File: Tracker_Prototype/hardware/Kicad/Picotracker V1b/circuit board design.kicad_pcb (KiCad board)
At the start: 2 copper layers, 33.3 x 20.1 mm, 30 parts, among them J1 Conn_01x06, J2 GND, J3 3.3V, SW1 SW_Push, U1 MAX-M8C, U3 CMWX1ZZABZ-078, U6 MS5607-02BA

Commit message: updated the "b" variant
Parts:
- removed AE2: GPS Antenna, Connector_Wire:SolderWirePad_1x01_Drill0.8mm
- removed C12: 100nF, Capacitor_SMD:C_0402_1005Metric
- removed C13: 10uF, Capacitor_SMD:C_0603_1608Metric
- removed G***: LOGO, flight-computer:ICSS_Logo
- removed R1, R2: 100K, Resistor_SMD:R_0402_1005Metric
- removed U1: MAX-M8C, RF_GPS:ublox_MAX
- added IC7: SPV1040, Package_SO:TSSOP-8_4.4x3mm_P0.65mm, F.Cu at (286.9, 151.4)
- added J4: Conn_01x01, Connector_PinHeader_1.27mm:PinHeader_1x01_P1.27mm_Vertical, F.Cu at (293.5, 150.8)
- J3: value 3.3V -> +SOL
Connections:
- J3 pad 1: +3V3 -> +SOL
- U3 pad 15: /GPS_TIMEPULSE -> (no net)
- U3 pad 16: /GPS_EXTINT -> (no net)
- U3 pad 17: /GPS_SAFEBOOT -> (no net)
- U3 pad 24: /V_SOLAR -> (no net)
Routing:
- net /GPS_EXTINT: track 10.0 -> 0.00 mm
- net /GPS_SAFEBOOT: track 9.36 -> 0.00 mm
- net /GPS_TIMEPULSE: track 8.59 -> 0.00 mm
- net GND: track 79.3 -> 72.8 mm
- net Net-(AE2-Pad1): track 6.23 -> 0.00 mm
- net /V_SOLAR: track 4.84 -> 0.00 mm
- net (no net): track 0.00 -> 4.84 mm
- net /I2C1_SCL: track 26.8 -> 23.3 mm
- net +3V3: track 79.5 -> 77.1 mm

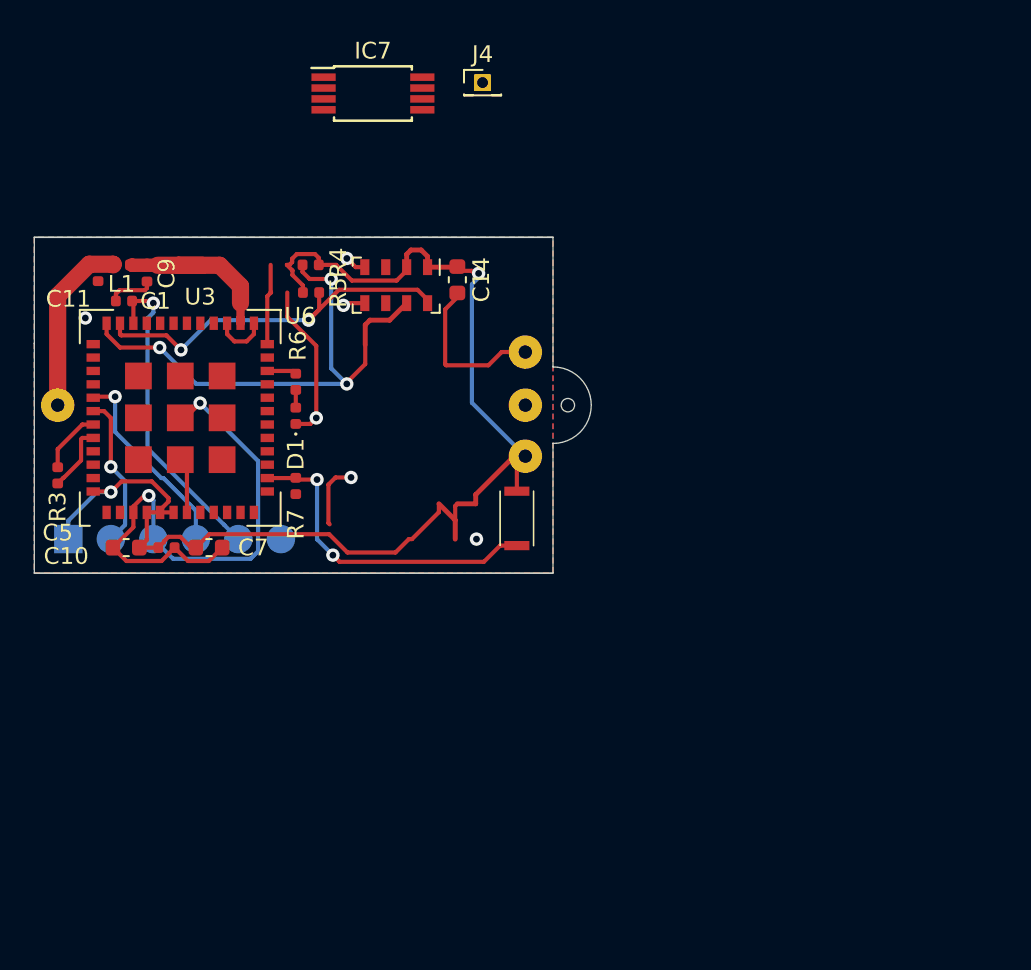
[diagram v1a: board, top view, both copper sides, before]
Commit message: mostly wired up the "b" variant. Changed the fill clearance for copper pour for the "a" variant to a much smaller 0.15mm
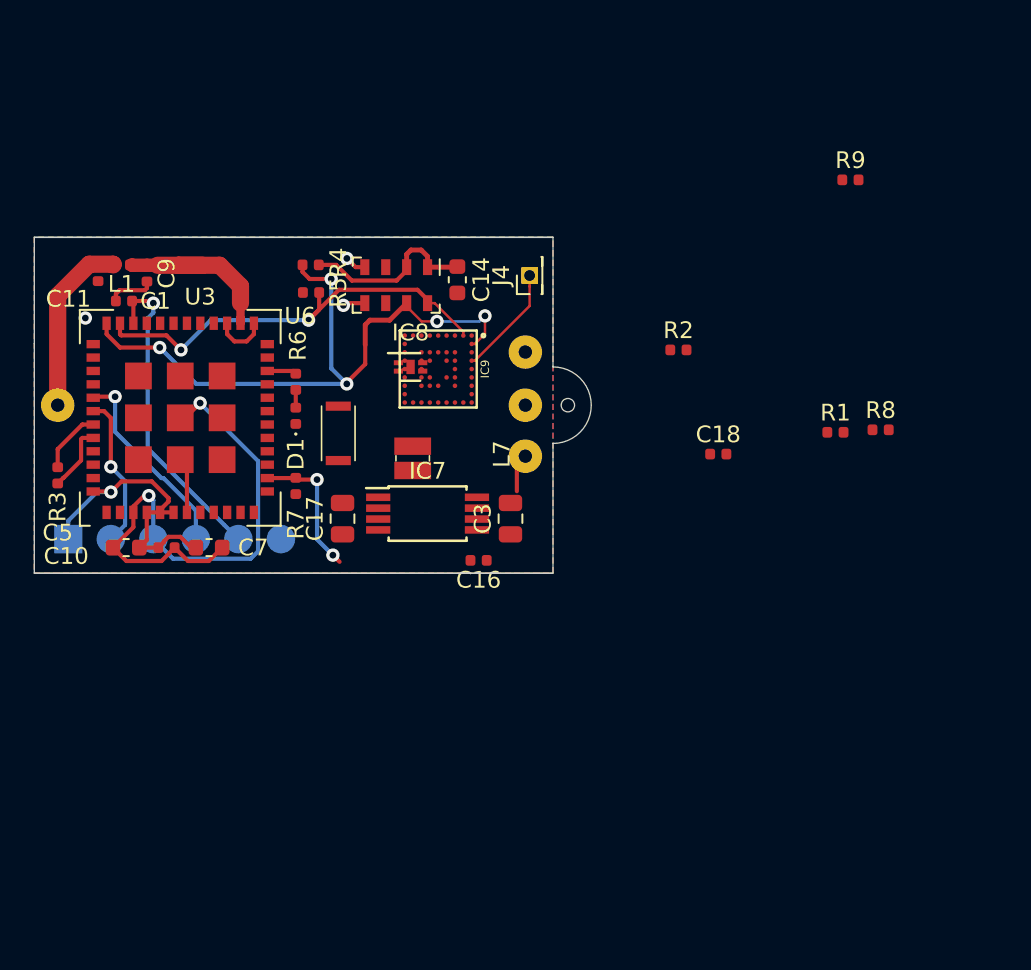
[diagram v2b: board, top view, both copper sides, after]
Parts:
- added C16: 1n, Capacitor_SMD:C_0402_1005Metric, F.Cu at (293.2, 179.3)
- added C17: 22u, Capacitor_SMD:C_0805_2012Metric, F.Cu at (285.1, 176.8)
- added C18: 100n, Capacitor_SMD:C_0402_1005Metric, F.Cu at (307.6, 173.0)
- added C3: 22u, Capacitor_SMD:C_0805_2012Metric, F.Cu at (295.1, 176.8)
- added IC8: SIP32431DNP3-T1GE4, pecanpico:DFN-4-1EP_1.2x1.6mm_P0.5mm_EP, F.Cu at (289.2, 167.8)
- added IC9: ZOE-M8G/B, pecanpico:ZOE-M8, F.Cu at (290.8, 167.9)
- added L7: XFL2006-472MEB, pecanpico:XFL20xx, F.Cu at (289.3, 173.2)
- added R1: R, Resistor_SMD:R_0402_1005Metric, F.Cu at (314.6, 171.7)
- added R2: 10K, Resistor_SMD:R_0402_1005Metric, F.Cu at (305.2, 166.8)
- added R8: R, Resistor_SMD:R_0402_1005Metric, F.Cu at (317.3, 171.5)
- added R9: 10K, Resistor_SMD:R_0402_1005Metric, F.Cu at (315.5, 156.6)
- moved IC7 25.3 mm to (290.2, 176.5)
- moved J4 11.9 mm to (296.3, 162.3), turned to 90 degrees
- moved SW1 11.8 mm to (284.9, 172.2)
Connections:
- IC7 pad 3: (no net) -> Net-(IC7-Pad3)
- IC7 pad 5: (no net) -> Net-(C16-Pad2)
- J4 pad 1: (no net) -> Net-(IC9-PadA4)
- U3 pad 16: (no net) -> /GPS_EXTINT
- U3 pad 17: (no net) -> /GPS_SAFEBOOT
- U3 pad 24: (no net) -> /V_SOLAR
- U3 pad 38: (no net) -> /GPS_EN
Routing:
- net +3V3: track 77.1 -> 29.0 mm, vias 2 -> 1
- net GND: track 72.8 -> 49.8 mm, vias 8 -> 5
- net /SWITCH: track 19.5 -> 8.49 mm
- net /I2C1_SDA: track 32.2 -> 39.7 mm, vias 3 -> 5
- net Net-(IC9-PadA4): track 0.00 -> 6.63 mm
- net (no net): track 4.84 -> 0.00 mm
- net /I2C1_SCL: track 23.3 -> 26.3 mm
- net +SOL: track 0.00 -> 2.30 mm
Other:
- rule trace_min: 0.2 -> 0.15
- rule via_min_drill: 0.3 -> 0.2
- rule via_min_size: 0.4 -> 0.45

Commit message: updated circuit of b variant for low power voltage measurment. Made a variant tcxo enable controllable
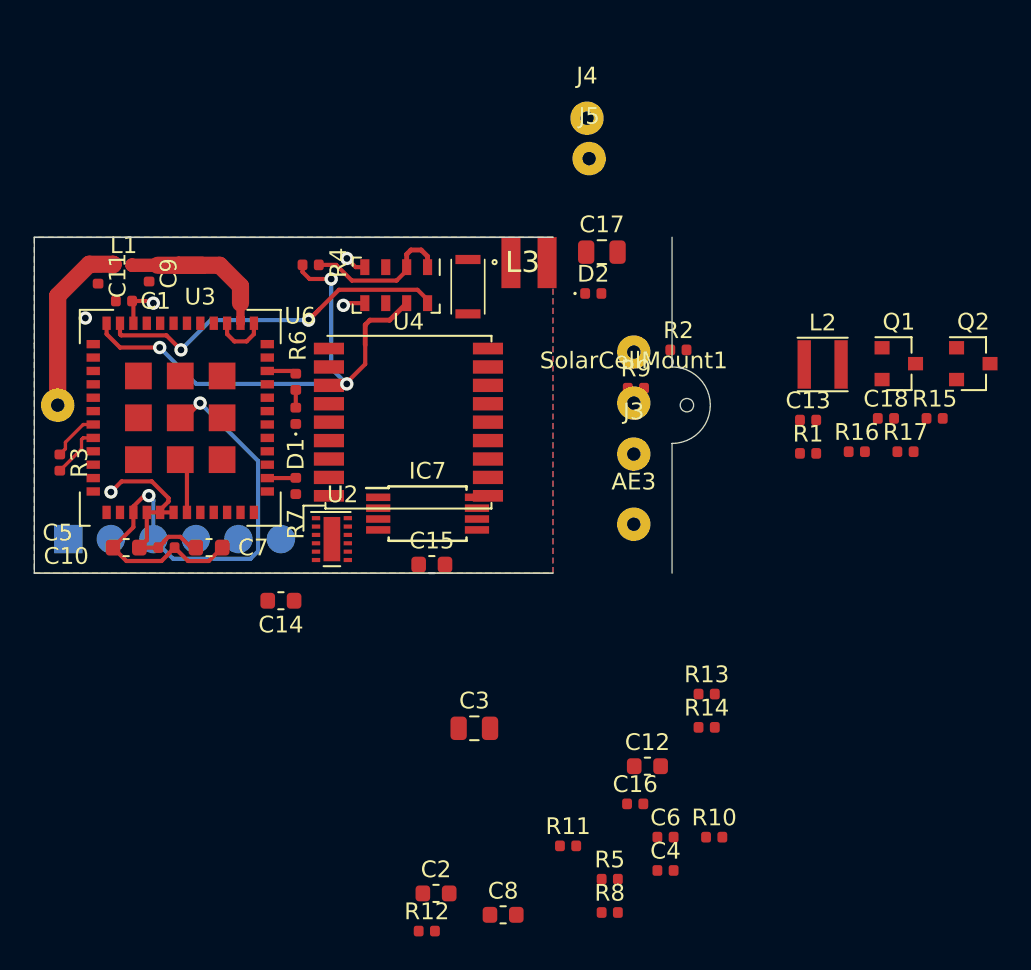
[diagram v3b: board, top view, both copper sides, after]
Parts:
- removed IC8: SIP32431DNP3-T1GE4, pecanpico:DFN-4-1EP_1.2x1.6mm_P0.5mm_EP
- removed IC9: ZOE-M8G/B, pecanpico:ZOE-M8
- removed L7: XFL2006-472MEB, pecanpico:XFL20xx
- added AE3: GPS Antenna, Connector_Wire:SolderWirePad_1x01_Drill0.8mm, F.Cu at (302.5, 177.2)
- added C12: 10uF, Capacitor_SMD:C_0603_1608Metric, F.Cu at (303.3, 191.6)
- added C13: 100nF, Capacitor_SMD:C_0402_1005Metric, F.Cu at (312.9, 170.9)
- added C15: 1uF, Capacitor_SMD:C_0603_1608Metric, F.Cu at (290.4, 179.6)
- added C2: 10uF, Capacitor_SMD:C_0603_1608Metric, F.Cu at (290.7, 199.2)
- added C4: 1nF, Capacitor_SMD:C_0402_1005Metric, F.Cu at (304.4, 197.9)
- added C6: 100nF, Capacitor_SMD:C_0402_1005Metric, F.Cu at (304.4, 195.9)
- added C8: 10uF, Capacitor_SMD:C_0603_1608Metric, F.Cu at (294.7, 200.5)
- added D2: D_Schottky, Diode_SMD:D_0402_1005Metric, F.Cu at (300.1, 163.4)
- added J5: BATT_GND, Connector_Wire:SolderWirePad_1x01_Drill0.8mm, F.Cu at (299.8, 155.3)
- added L2: 2.2uH, Inductor_SMD:L_Taiyo-Yuden_NR-30xx, F.Cu at (313.8, 167.6)
- added L3: 10uH, Inductor_coilcraft:LPS3015, F.Cu at (296.3, 161.5)
- added Q1: Q_PMOS_DGS, Package_TO_SOT_SMD:SOT-23, F.Cu at (318.3, 167.6)
- added Q2: Q_PMOS_DGS, Package_TO_SOT_SMD:SOT-23, F.Cu at (322.8, 167.6)
- added R10: 1K, Resistor_SMD:R_0402_1005Metric, F.Cu at (307.3, 195.9)
- added R11: 1K, Resistor_SMD:R_0402_1005Metric, F.Cu at (298.6, 196.4)
- added R12: 1Ohm, Resistor_SMD:R_0402_1005Metric, F.Cu at (290.1, 201.5)
- added R13: 10M, Resistor_SMD:R_0402_1005Metric, F.Cu at (306.9, 187.3)
- added R14: 5.1M, Resistor_SMD:R_0402_1005Metric, F.Cu at (306.9, 189.3)
- added R15: 100K, Resistor_SMD:R_0402_1005Metric, F.Cu at (320.5, 170.8)
- added R16: 100K, Resistor_SMD:R_0402_1005Metric, F.Cu at (315.8, 172.8)
- added R17: 10K, Resistor_SMD:R_0402_1005Metric, F.Cu at (318.7, 172.8)
- added U2: TPS62740, Package_SON:WSON-12-1EP_3x2mm_P0.5mm_EP1x2.65, F.Cu at (284.5, 178.1)
- added U4: MAX-M8C, RF_GPS:ublox_MAX, F.Cu at (289.1, 171.1)
- C16: value 1n -> 1nF
- C17: value 22u -> 22uF
- C18: value 100n -> 100nF
- C3: value 22u -> 4.7uF
- J1: footprint femto_footprints:special_test_pads -> flight-computer:special_test_pads
- J4: value Conn_01x01 -> BATT_V+; footprint Connector_PinHeader_1.27mm:PinHeader_1x01_P1.27mm_Vertical -> Connector_Wire:SolderWirePad_1x01_Drill0.8mm
- R1: value R -> 10K
- R2, R9: value 10K -> 100K
- R8: value R -> 1K
- moved R5 39.3 mm to (301.1, 198.4)
- moved R8 33.1 mm to (301.1, 200.4)
- moved C17 22.2 mm to (300.6, 160.9), turned to 0 degrees
- moved C14 21.9 mm to (281.4, 181.7), turned to 180 degrees
- moved R9 17.9 mm to (302.6, 169.0)
- moved C16 17.3 mm to (302.6, 193.9), turned to 0 degrees
- moved C3 12.7 mm to (293.0, 189.4), turned to 0 degrees
- moved SW1 11.7 mm to (292.6, 163.4)
- moved C18 10.2 mm to (317.6, 170.8)
- moved J4 10.0 mm to (299.7, 152.9), turned to 0 degrees
- moved StringHole1 7.11 mm to (305.7, 170.1)
- moved J3 6.48 mm to (302.5, 173.0), turned to 0 degrees
- moved SolarCellMount1 6.48 mm to (302.5, 169.9), turned to 0 degrees
- moved J2 6.48 mm to (302.5, 166.9)
- moved R1 2.06 mm to (312.9, 172.9)
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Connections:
- net /V_SOLAR renamed /SOLAR_VOLTS
- C10 pad 1: +3V3 -> VCC
- C14 pad 1: +3V3 -> VCC
- C16 pad 1: GND -> Net-(C16-Pad1)
- C16 pad 2: Net-(C16-Pad2) -> GND
- C17 pad 1: +3V3 -> GND
- C17 pad 2: GND -> Net-(C17-Pad2)
- C18 pad 1: +GPS -> Net-(C18-Pad1)
- C18 pad 2: GND -> /SOL_PWR_MEASURE
- C5 pad 1: +3V3 -> VCC
- C7 pad 1: +3V3 -> VCC
- IC7 pad 1: +SOL -> Net-(C4-Pad1)
- IC7 pad 4: +3V3 -> Net-(C17-Pad2)
- IC7 pad 5: Net-(C16-Pad2) -> Net-(C16-Pad1)
- IC7 pad 6: +3V3 -> Net-(C15-Pad2)
- IC7 pad 7: +3V3 -> Net-(C15-Pad1)
- IC7 pad 8: +SOL -> (no net)
- J1 pad 1: +3V3 -> VCC
- J4 pad 1: Net-(IC9-PadA4) -> +BATT
- R1 pad 1: Net-(C16-Pad2) -> +BATT
- R1 pad 2: +3V3 -> Net-(C13-Pad1)
- R2 pad 1: +SOL -> Net-(Q2-Pad1)
- R4 pad 1: +3V3 -> VCC
- R5 pad 1: +3V3 -> VCC
- R8 pad 1: GND -> +SOL
- R8 pad 2: Net-(C16-Pad2) -> Net-(C4-Pad1)
- SW1 pad 2: +3V3 -> VCC
- U3 pad 15: (no net) -> /GPS_TIMEPULSE
- U3 pad 18: (no net) -> /SOL_PWR_MEASURE
- U3 pad 19: (no net) -> /BATT_PWR_MEASURE
- U3 pad 23: (no net) -> /BATT_VOLTS
- U3 pad 38: /GPS_EN -> /SENSOR_EN
- U3 pad 4: +3V3 -> VCC
- U3 pad 40: (no net) -> /TCXO_EN
- U3 pad 48: +3V3 -> /TCXO_EN
- U3 pad 5: +3V3 -> VCC
- U3 pad 6: +3V3 -> VCC
- U6 pad 1: +3V3 -> VCC
- U6 pad 2: +3V3 -> VCC
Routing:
- net +3V3: track 29.0 -> 0.00 mm, vias 1 -> 0
- net VCC: track 0.00 -> 22.1 mm, vias 0 -> 1
- net /RESET: track 19.2 -> 2.68 mm
- net /SWDIO: track 11.9 -> 0.09 mm, vias 1 -> 0
- net /SWCLK: track 9.17 -> 0.00 mm, vias 1 -> 0
- net /I2C1_SDA: track 39.7 -> 32.4 mm, vias 5 -> 3
- net /SWITCH: track 8.49 -> 1.85 mm, vias 2 -> 0
- net Net-(IC9-PadA4): track 6.63 -> 0.00 mm
- net /I2C1_SCL: track 26.3 -> 22.3 mm
- net GND: track 49.8 -> 46.1 mm
- net +SOL: track 2.30 -> 0.00 mm
- net Net-(R3-Pad1): track 3.81 -> 2.97 mm
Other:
- board size 33.3 x 20.1 mm -> 40.4 x 20.1 mm

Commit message: Routed most of the b variant of the board
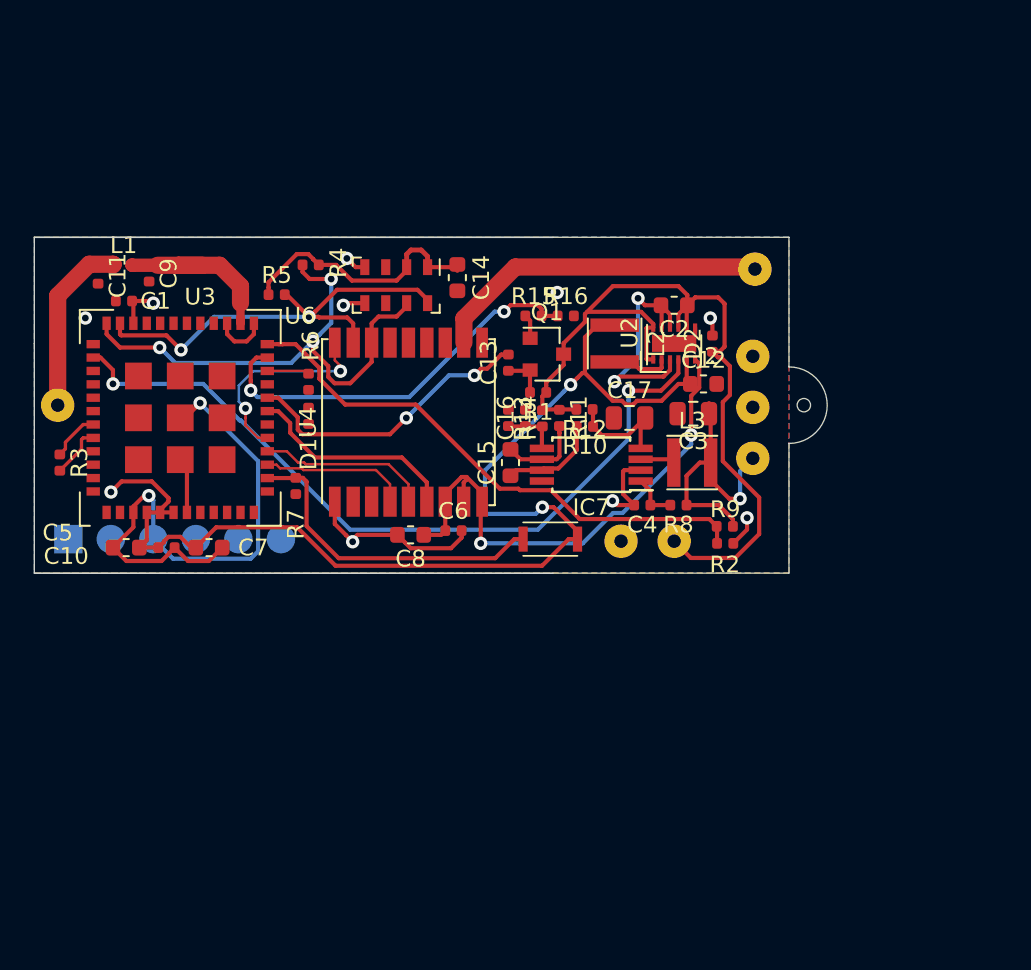
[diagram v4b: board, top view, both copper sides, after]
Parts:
- removed C18: 100nF, Capacitor_SMD:C_0402_1005Metric
- removed Q2: Q_PMOS_DGS, Package_TO_SOT_SMD:SOT-23
- removed R17: 10K, Resistor_SMD:R_0402_1005Metric
- added J6: ICSS LOGO, flight-computer:ICSS_Logo, B.Cu at (280.2, 165.7)
- AE3, J2, J3, J4, J5, SolarCellMount1: moved to B.Cu
- L3: footprint Inductor_coilcraft:LPS3015 -> Inductor_SMD:L_Taiyo-Yuden_NR-30xx
- moved R5 40.2 mm to (281.2, 163.4)
- moved C2 37.9 mm to (304.9, 164.1), turned to 180 degrees
- moved R12 32.6 mm to (299.6, 170.3), turned to 180 degrees
- moved J4 25.8 mm to (304.9, 178.2), turned to 90 degrees
- moved R10 25.7 mm to (299.6, 171.3), turned to 180 degrees
- moved R11 25.6 mm to (298.1, 170.8), turned to 270 degrees
- moved R15 24.7 mm to (296.5, 164.7)
- moved R8 24.7 mm to (305.2, 176.0), turned to 180 degrees
- moved C16 24.0 mm to (296.0, 170.8), turned to 90 degrees
- moved U2 23.5 mm to (304.9, 166.4), turned to 90 degrees
- moved C8 23.4 mm to (289.2, 177.8), turned to 180 degrees
- moved C12 23.1 mm to (306.7, 168.8)
- moved J5 22.9 mm to (301.8, 178.2), turned to 90 degrees
- moved C3 22.9 mm to (306.1, 170.6), turned to 180 degrees
- moved C6 22.3 mm to (291.7, 177.5)
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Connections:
- C14 pad 1: VCC -> SENSOR_VCC
- C6 pad 1: VCC -> SENSOR_VCC
- C8 pad 1: VCC -> SENSOR_VCC
- R2 pad 1: Net-(Q2-Pad1) -> +SOL
- R4 pad 1: VCC -> SENSOR_VCC
- R5 pad 1: VCC -> SENSOR_VCC
- U2 pad 10: +BATT -> GND
- U2 pad 11: +BATT -> GND
- U2 pad 6: VCC -> SENSOR_VCC
- U2 pad 8: GND -> +BATT
- U2 pad 9: GND -> +BATT
- U3 pad 18: /SOL_PWR_MEASURE -> (no net)
- U3 pad 19: /BATT_PWR_MEASURE -> /GPS_BCKP
- U3 pad 20: (no net) -> /BATT_PWR_MEASURE
- U4 pad 6: VCC -> /GPS_BCKP
- U4 pad 7: VCC -> SENSOR_VCC
- U4 pad 8: VCC -> SENSOR_VCC
- U4 pad 9: VCC -> SENSOR_VCC
- U6 pad 1: VCC -> SENSOR_VCC
- U6 pad 2: VCC -> SENSOR_VCC
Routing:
- net +BATT: track 0.00 -> 51.1 mm
- net SENSOR_VCC: track 0.00 -> 47.2 mm, vias 0 -> 2
- net VCC: track 22.1 -> 69.1 mm, vias 1 -> 3
- net /SENSOR_EN: track 0.00 -> 46.1 mm, vias 0 -> 2
- net /SOLAR_VOLTS: track 0.00 -> 33.0 mm
- net GND: track 46.1 -> 78.7 mm, vias 5 -> 12
- net /BATT_VOLTS: track 0.00 -> 24.0 mm, vias 0 -> 2
- net Net-(AE3-Pad1): track 0.00 -> 20.2 mm
- net /BATT_PWR_MEASURE: track 0.00 -> 17.7 mm, vias 0 -> 2
- net /SWITCH: track 1.85 -> 19.5 mm
- net +SOL: track 0.00 -> 16.0 mm, vias 0 -> 1
- net /GPS_BCKP: track 0.00 -> 12.8 mm
- net /GPS_SAFEBOOT: track 0.00 -> 12.4 mm, vias 0 -> 2
- net /GPS_EXTINT: track 0.00 -> 10.3 mm
- net /GPS_TIMEPULSE: track 0.00 -> 8.86 mm
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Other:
- board size 40.4 x 20.1 mm -> 47.4 x 20.1 mm

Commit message: Finished the routing of the b variant.
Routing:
- net SENSOR_VCC: track 47.2 -> 68.7 mm, vias 2 -> 4
- net /RESET: track 2.68 -> 22.3 mm
- net /SWDIO: track 0.09 -> 11.7 mm, vias 0 -> 1
- net /TCXO_EN: track 0.00 -> 9.99 mm
- net /SWCLK: track 0.00 -> 9.12 mm, vias 0 -> 1
- net VCC: track 69.1 -> 78.0 mm
- net GND: track 78.7 -> 84.0 mm, vias 12 -> 15
- net (no net): track 1.94 -> 0.00 mm
- net Net-(D1-Pad2): track 0.00 -> 1.06 mm
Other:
- outline, holes or cut-outs redrawn

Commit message: Routed most of the swaped config board
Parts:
- moved R2 28.7 mm to (282.1, 164.8), turned to 270 degrees
- moved R9 28.4 mm to (282.1, 166.8), turned to 270 degrees
- moved U4 13.7 mm to (302.8, 171.2)
- moved C8 13.3 mm to (302.5, 177.9)
- moved C6 13.3 mm to (305.1, 177.7)
- moved R5 13.1 mm to (294.3, 162.2), turned to 270 degrees
- moved C14 11.4 mm to (303.4, 162.7)
- moved U6 11.4 mm to (299.8, 163.1)
- moved C13 11.1 mm to (284.0, 168.8), turned to 180 degrees
- moved R15 11.1 mm to (285.5, 165.2)
- moved R16 11.1 mm to (287.4, 165.2)
- moved C12 10.8 mm to (295.9, 169.3)
- moved C15 10.7 mm to (284.5, 174.0)
- moved C17 10.7 mm to (291.6, 171.3)
- moved C2 10.7 mm to (294.3, 164.6)
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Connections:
- U3 pad 17: /GPS_SAFEBOOT -> (no net)
- U3 pad 22: /LED -> /BATT_VOLTS
- U3 pad 23: /BATT_VOLTS -> /SOLAR_VOLTS
- U3 pad 24: /SOLAR_VOLTS -> /LED
- U4 pad 18: /GPS_SAFEBOOT -> (no net)
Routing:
- net GND: track 84.0 -> 37.5 mm, vias 15 -> 5
- net +SOL: track 16.0 -> 50.2 mm, vias 1 -> 2
- net /SOLAR_VOLTS: track 33.0 -> 2.77 mm
- net /SENSOR_EN: track 45.8 -> 28.1 mm
- net /GPS_EXTINT: track 10.3 -> 27.5 mm, vias 0 -> 2
- net VCC: track 78.0 -> 61.0 mm
- net /GPS_TIMEPULSE: track 8.86 -> 25.4 mm, vias 0 -> 2
- net /GPS_BCKP: track 12.8 -> 28.6 mm, vias 0 -> 2
- net /BATT_VOLTS: track 24.0 -> 9.42 mm, vias 2 -> 0
- net /BATT_PWR_MEASURE: track 17.7 -> 3.21 mm, vias 2 -> 0
- net SENSOR_VCC: track 68.7 -> 54.5 mm
- net /I2C1_SDA: track 31.5 -> 44.0 mm, vias 3 -> 2
- net Net-(AE3-Pad1): track 20.2 -> 7.69 mm
- net /GPS_SAFEBOOT: track 12.4 -> 0.00 mm, vias 2 -> 0
- net /I2C1_SCL: track 27.3 -> 39.6 mm
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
